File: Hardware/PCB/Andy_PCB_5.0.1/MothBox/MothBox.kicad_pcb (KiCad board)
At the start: 2 copper layers, 237 x 140.5 mm, 135 parts, among them J1 DB141V-2.54-4P, J2 DB141V-2.54-4P, J3 DB141V-2.54-4P, J4 DB141V-2.54-4P, Q1 JMTV210P02A, Q12 YJQ10N2A, Q2 BC817, Q3 YJQ10N2A, Q4 YJQ10N2A, Q5 YJQ10N2A, Q6 YJQ10N2A, Q7 YJQ10N2A, Q8 JMTV210P02A, U10 Days, U11 Modes, U13 Hours1, U14 Hours2, U15 PCA9535PW, U16 PCA9535PW, U19 graphic, U2 XL4015E1, U3 INA219BIDCNT, U5 RASPBERRY_PI_5, U6 RASPBERRY_PI_4B_4GB, U7 Female Inv Socket Pi 2.54-2*20, U8 GPs 5 pin PM2.54-1*5

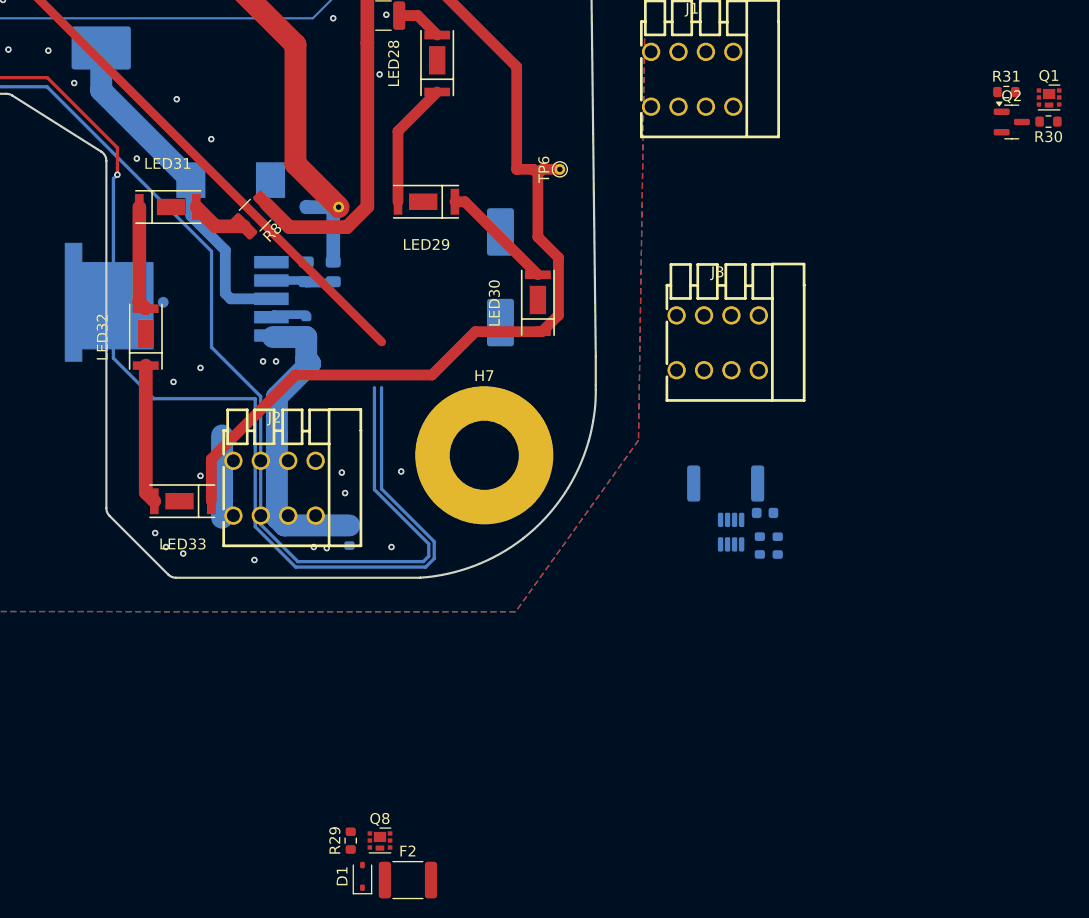
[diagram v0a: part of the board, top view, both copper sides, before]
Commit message: adding in datasheets
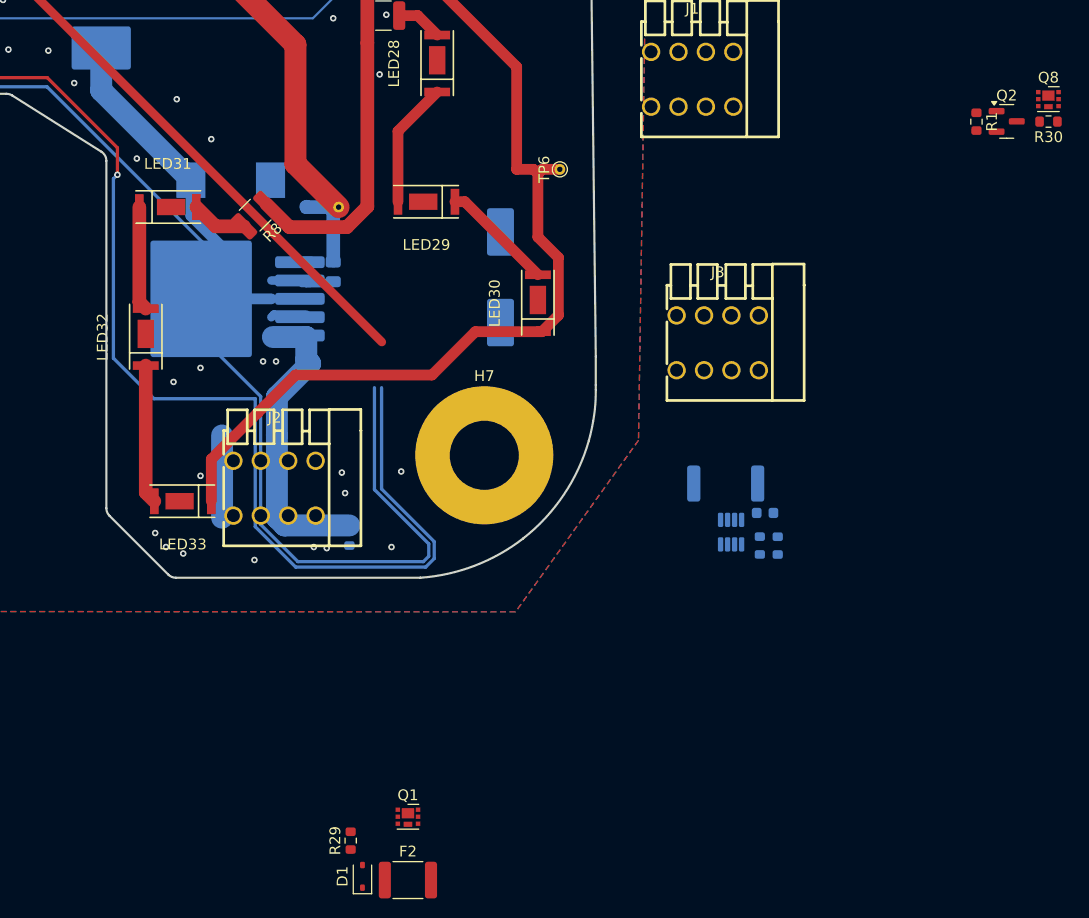
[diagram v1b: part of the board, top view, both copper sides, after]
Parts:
- removed R31: 1K, MothBox_footprints_Library:R_0603_1608Metric
- added R1: 10K, MothBox_footprints_Library:R_0603_1608Metric, F.Cu at (303.6, 161.3)
- Q2: value BC817 -> AO3400A
- U2: footprint MothBox_footprints_Library:TO-263-5_L10.2-W8.9-P1.70-TL -> Package_TO_SOT_SMD:TO-263-5_TabPin3
- moved Q8 92.5 mm to (310.3, 159.3)
- moved Q1 89.3 mm to (250.9, 225.8)
- moved Q2 0.47 mm to (306.4, 161.3)
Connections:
- Q1 pad 1: Net-(Q1-G) -> Net-(D1-A)
- Q1 pad 2: +24V -> Net-(D1-K)
- Q1 pad 3: Net-(J3-Pin_3) -> Net-(J2-Pin_3)
- Q2 pad 1: Net-(Q2-B) -> EN_12VReg
- Q2 pad 3: Net-(Q1-G) -> Net-(Q2-D)
- Q8 pad 1: Net-(D1-A) -> Net-(Q2-D)
- Q8 pad 2: Net-(D1-K) -> +24V
- Q8 pad 3: Net-(J2-Pin_3) -> Net-(J3-Pin_3)
- R30 pad 2: Net-(Q1-G) -> Net-(Q2-D)

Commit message: rough outline of PCB. Lots of tidying up needed
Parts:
- removed Q12: YJQ10N2A, MothBox_footprints_Library:DFN2020-3
- removed R28: 10k, MothBox_footprints_Library:R_0805_2012Metric
- added C8: 10uF, MothBox_footprints_Library:C_0603_1608Metric, B.Cu at (253.2, 176.2)
- added Q9: YJQ10N2A, MothBox_footprints_Library:U-DFN2020-6_L2.0-W2.0-P0.65-BL, B.Cu at (199.2, 80.6)
- added R31: 10K, MothBox_footprints_Library:R_0603_1608Metric, B.Cu at (107.3, 70.1)
- added TP2: 24V_test, MothBox_footprints_Library:TestPoint_THTPad_D1.0mm_Drill0.5mm, F.Cu at (253.3, 172.9)
- added TP5: 12V_test, MothBox_footprints_Library:TestPoint_THTPad_D1.0mm_Drill0.5mm, F.Cu at (240.6, 165.3)
- added TP7: 3V3_test, MothBox_footprints_Library:TestPoint_THTPad_D1.0mm_Drill0.5mm, F.Cu at (204.9, 141.7)
- D1, D2, D5, D6, D7, F2, Q2, R1, R29, R30: moved to B.Cu
- Q1, Q4, Q5, Q6, Q8: footprint MothBox_footprints_Library:DFN2020-3 -> MothBox_footprints_Library:U-DFN2020-6_L2.0-W2.0-P0.65-BL; moved to B.Cu
- Q3, Q7: footprint MothBox_footprints_Library:DFN2020-3 -> MothBox_footprints_Library:U-DFN2020-6_L2.0-W2.0-P0.65-BL
- R11, R9: value 10k -> 10K; footprint MothBox_footprints_Library:R_0805_2012Metric -> MothBox_footprints_Library:R_0603_1608Metric
- R19, R21, R27: value 10k -> 10K; footprint MothBox_footprints_Library:R_0805_2012Metric -> MothBox_footprints_Library:R_0603_1608Metric; moved to B.Cu
- moved Q3 189.6 mm to (104.6, 119.6), turned to 90 degrees
- moved R11 185.7 mm to (104.6, 117.5), turned to 180 degrees
- moved H9 127.4 mm to (102.4, 70.5), turned to -90 degrees
- moved Q5 119.8 mm to (250.0, 78.8), turned to -90 degrees
- moved D7 118.0 mm to (107.3, 68.2)
- moved R27 89.7 mm to (250.0, 80.8), turned to 180 degrees
- moved D6 89.3 mm to (250.0, 82.7), turned to 180 degrees
- moved D2 89.2 mm to (199.2, 84.7)
- moved Q6 88.5 mm to (107.3, 72.2), turned to 90 degrees
- moved Q7 81.6 mm to (226.2, 118.3), turned to 90 degrees
- moved H8 80.7 mm to (252.6, 70.7), turned to -90 degrees
- moved R21 77.6 mm to (199.2, 82.8), turned to 180 degrees
- moved R9 70.3 mm to (226.2, 116.3), turned to 180 degrees
- moved H10 67.9 mm to (198.9, 70.8), turned to -90 degrees
- moved Q8 64.0 mm to (247.9, 173.6)
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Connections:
- H10 pad 1: +12V -> unconnected-(H10-Pad1)
- H10 pad 2: unconnected-(H10-Pad2) -> +12V
- H10 pad 3: +12V -> unconnected-(H10-Pad3)
- H10 pad 4: unconnected-(H10-Pad4) -> +12V
- H10 pad 5: Net-(H10-Pad5) -> unconnected-(H10-Pad5)
- H10 pad 6: unconnected-(H10-Pad6) -> Net-(H10-Pad6)
- H10 pad 7: Net-(H10-Pad5) -> unconnected-(H10-Pad7)
- H10 pad 8: unconnected-(H10-Pad8) -> Net-(H10-Pad6)
- J3 pad 1: Net-(J3-Pin_1) -> GND
- J3 pad 2: Net-(J3-Pin_1) -> GND
- Q1 pad 1: Net-(D1-A) -> Net-(J2-Pin_3)
- Q1 pad 2: Net-(D1-K) -> Net-(J2-Pin_3)
- Q1 pad 3: Net-(J2-Pin_3) -> Net-(D1-A)
- Q3 pad 1: Net-(LED27-K) -> Net-(LED12-K)
- Q3 pad 2: Net-(LED27-K) -> Net-(LED12-K)
- Q3 pad 3: Net-(LED27-K) -> PHOTO_LED_CTRL
- Q4 pad 3: Net-(J4-Pin_1) -> UV4_EX_CTRL
- Q5 pad 1: Net-(H10-Pad5) -> Net-(H8-Pad6)
- Q5 pad 2: Net-(H10-Pad5) -> Net-(H8-Pad6)
- Q5 pad 3: Net-(H10-Pad5) -> UV1_CTRL
- Q6 pad 1: Net-(H8-Pad6) -> Net-(H9-Pad6)
- Q6 pad 2: Net-(H8-Pad6) -> Net-(H9-Pad6)
- Q6 pad 3: Net-(H8-Pad6) -> UV3_CTRL
- Q7 pad 1: Net-(H9-Pad6) -> Net-(LED27-K)
- Q7 pad 2: Net-(H9-Pad6) -> Net-(LED27-K)
- Q7 pad 3: Net-(H9-Pad6) -> PHOTO_LED_CTRL
- Q8 pad 1: Net-(Q2-D) -> Net-(J3-Pin_3)
- Q8 pad 2: +24V -> Net-(J3-Pin_3)
- Q8 pad 3: Net-(J3-Pin_3) -> Net-(Q2-D)
- R11 pad 1: GND -> PHOTO_LED_CTRL
- R11 pad 2: PHOTO_LED_CTRL -> GND
- R19 pad 1: GND -> UV4_EX_CTRL
- R19 pad 2: UV4_EX_CTRL -> GND
- R21 pad 1: GND -> UV2_CTRL
- R21 pad 2: UV2_CTRL -> GND
- R27 pad 1: GND -> UV1_CTRL
- R27 pad 2: UV1_CTRL -> GND
- R9 pad 1: GND -> PHOTO_LED_CTRL
- R9 pad 2: PHOTO_LED_CTRL -> GND
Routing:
- net +3.3V: track 268.4 -> 392.5 mm, vias 1 -> 5
- net (no net): track 118.5 -> 0.00 mm, vias 1 -> 0
- net unconnected-(U7-Pad34): track 110.6 -> 0.00 mm, vias 4 -> 0
- net GND: track 29.4 -> 123.9 mm, vias 372 -> 371
- net EN_12VReg: track 245.2 -> 326.6 mm, vias 0 -> 2
- net unconnected-(U7-Pad14): track 62.1 -> 0.00 mm, vias 4 -> 0
- net UV2_CTRL: track 79.3 -> 123.1 mm
- net SCL: track 576.0 -> 537.6 mm, vias 11 -> 13
- net Net-(J3-Pin_3): track 0.00 -> 33.2 mm
- net unconnected-(U7-Pad16): track 31.9 -> 0.00 mm, vias 2 -> 0
- net Net-(LED14-K): track 35.9 -> 5.87 mm
- net Net-(J2-Pin_3): track 0.00 -> 26.2 mm
- net UV1_CTRL: track 172.7 -> 195.2 mm, vias 3 -> 2
- net +24V: track 29.0 -> 50.9 mm
- net SDA: track 575.2 -> 553.6 mm, vias 9 -> 11
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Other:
- board text added: "12V"
- board text added: "24V"
- board text added: "3V3"
- board text added: "5V"
- board text added: "PHOTO LED CTL"
- board text added: "PHOTO LED GND"
- board text added: "Photo LEDs"
